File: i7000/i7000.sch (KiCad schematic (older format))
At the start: 31 parts, among them CN04 Conn_02x30_Counter_Clockwise, CN05 Conn_02x07_Counter_Clockwise

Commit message: transcricao de ontem de madrugada
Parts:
- added CI01: 2732, symbol memory:2732
- added CI02: 6116, symbol memory:6116
- added CI06: 74LS240, symbol Logic_74xx:74LS240
- added CI09: 74LS38, symbol Logic_74xx:74LS38
- added CI12: 74LS139, symbol Logic_74xx:74LS139
- added CI13: 74LS273, symbol Logic_74xx:74LS273
- added CI14: 74LS138, symbol Logic_74xx:74LS138
- added CI15: 74LS21, symbol Logic_74xx:74LS21
- added CI16: 74LS123, symbol Logic_74xx:74LS123
- added CI17: 74LS244, symbol Logic_74xx:74LS244
- added CI19: 74LS04, symbol Logic_74xx:74LS04
- added CI21: 74LS00, symbol Logic_74xx:74LS00
- added CN01: Conn_02x30_Counter_Clockwise, symbol Connector:Conn_02x30_Counter_Clockwise
- added CN?: Conn_02x07_Counter_Clockwise, symbol Connector:Conn_02x07_Counter_Clockwise
- added E06: 74LS373, symbol Logic_74xx:74LS373
- added R41: R, symbol device:R
- added U?: 74LS245, symbol Logic_74xx:74LS245
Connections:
- net labels added: CN04_14, CN04_19, CN04_20, CN04_34, CN04_42, CN04_43, CN04_54, CPU_A10, CPU_A11, CPU_A12, CPU_A13, CPU_A14, CPU_A15, CPU_A8, CPU_A9, CPU_AD0, CPU_AD1, CPU_AD2, CPU_AD3, CPU_AD4, CPU_AD5, CPU_AD6, CPU_AD7, ~EPROM_E, ~FDC_CS, ~SRAM_CS, ~WE_CN04_40
- net labels removed: CN04_40
- wire segments 138 -> 272
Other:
- note added: "CI03 (Floppy Controller)\nTODO:\nDesenhar um\nsímbolo para\no WD2793A-PL2"
- note added: "TODO: symbol for NSC800.\nThis one has the Z80 pinout.\nOn the NSC800 the pinout is different."
- moved on the sheet: CN04, CN05, E08, E11, E13, E26B, E27F, E28F, E32C, E36B, F02, F03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

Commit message: mais um pouco hoje
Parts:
- added E02: Intel D8202A-1, symbol chips_not_yet_available_on_kicad:8202A
- added E05: 74LS373, symbol Logic_74xx:74LS373
- added E15: 74LS374, symbol Logic_74xx:74LS374
- added E29: 74LS04, symbol Logic_74xx:74LS04
- added unit 1 of E32
- gave numbers to parts that had none: 2
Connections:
- net labels added: A0, A1, A10, A11, A12, A13, A14, A15, A2, A3, A4, A5, A6, A7, A8, A9, E13_pin2
- net labels removed: CN04_17, DRAM_AH0, DRAM_AH1, DRAM_AH2, DRAM_AH3, DRAM_AH4, DRAM_AH5, DRAM_AL0, DRAM_AL1, DRAM_AL2, DRAM_AL3, DRAM_AL4, DRAM_AL5, DRAM_AL6
- wire segments 272 -> 359
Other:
- note added: "/FDC_CS = 0 when:\nA13 == 1\nA11 == 0\nA10 == 0\nCN04_14 == 0\nCN04_42 == 1\nCN04_43 == 1\n"
- note removed: "E02 (DRAM Controller)\nTODO:\nDesenhar um\nsímbolo para\no Intel D8202A-1"
- moved on the sheet: E09, E10, E13, E32C, E36B

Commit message: creating a library of symbols for chips used in the Itautec I7000 but still not available in KICAD libraries. We should contribute these later to the project.
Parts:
- removed E01: NSC800_CPU, symbol Zilog:Z80CPU
- added E01: NSC800D-4, symbol chips_not_yet_available_on_kicad:NSC800
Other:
- note removed: "TODO: symbol for NSC800.\nThis one has the Z80 pinout.\nOn the NSC800 the pinout is different."
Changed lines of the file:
@@
 	8850 7350 9000 7350
-$Comp
-L Zilog:Z80CPU E01
-U 1 1 5FD1F685
-P 5150 7150
-F 0 "E01" H 5150 8828 50  0000 C CNN
-F 1 "NSC800_CPU" H 5150 8737 50  0000 C CNN
-F 2 "" H 5150 7550 50  0001 C CNN
-F 3 "www.zilog.com/manage_directlink.php?filepath=docs/z80/um0080" H 5150 7550 50  0001 C CNN
-	1    5150 7150
-	1    0    0    -1
-$EndComp
 $Comp
 L Logic_74xx:74LS257 E08
@@
 	1    0    0    -1
 $EndComp
-Text Notes 4750 5450 0    31   ~ 0
-TODO: symbol for NSC800.\nThis one has the Z80 pinout.\nOn the NSC800 the pinout is different.
-Text GLabel 6000 5950 2    31   Output ~ 0
+Text GLabel 4800 5250 0    31   Output ~ 0
 CPU_AD0
 Wire Wire Line
-	5850 5950 6000 5950
-Text GLabel 6000 6050 2    31   Output ~ 0
+	4950 5250 4800 5250
+Text GLabel 4800 5350 0    31   Output ~ 0
 CPU_AD1
-Text GLabel 6000 6150 2    31   Output ~ 0
+Text GLabel 4800 5450 0    31   Output ~ 0
 CPU_AD2
-Text GLabel 6000 6250 2    31   Output ~ 0
+Text GLabel 4800 5550 0    31   Output ~ 0
 CPU_AD3
 Wire Wire Line
-	6000 6050 5850 6050
-Wire Wire Line
-	5850 6150 6000 6150
-Wire Wire Line
-	6000 6250 5850 6250
-Text GLabel 6000 6350 2    31   Output ~ 0
+	4800 5350 4950 5350
+Wire Wire Line
+	4950 5450 4800 5450
+Wire Wire Line
+	4800 5550 4950 5550
+Text GLabel 4800 5650 0    31   Output ~ 0
 CPU_AD4
 Wire Wire Line
-	5850 6350 6000 6350
-Text GLabel 6000 6450 2    31   Output ~ 0
+	4950 5650 4800 5650
+Text GLabel 4800 5750 0    31   Output ~ 0
 CPU_AD5
-Text GLabel 6000 6550 2    31   Output ~ 0
+Text GLabel 4800 5850 0    31   Output ~ 0
 CPU_AD6
-Text GLabel 6000 6650 2    31   Output ~ 0
+Text GLabel 4800 5950 0    31   Output ~ 0
 CPU_AD7
 Wire Wire Line
-	6000 6450 5850 6450
-Wire Wire Line
-	5850 6550 6000 6550
-Wire Wire Line
-	6000 6650 5850 6650
-Text GLabel 6000 6750 2    31   Output ~ 0
+	4800 5750 4950 5750
+Wire Wire Line
+	4950 5850 4800 5850
+Wire Wire Line
+	4800 5950 4950 5950
+Text GLabel 4800 6350 0    31   Output ~ 0
 CPU_A8
 Wire Wire Line
-	5850 6750 6000 6750
-Text GLabel 6000 6850 2    31   Output ~ 0
+	4950 6350 4800 6350
+Text GLabel 4800 6450 0    31   Output ~ 0
 CPU_A9
-Text GLabel 6000 6950 2    31   Output ~ 0
+Text GLabel 4800 6550 0    31   Output ~ 0
 CPU_A10
-Text GLabel 6000 7050 2    31   Output ~ 0
+Text GLabel 4800 6650 0    31   Output ~ 0
 CPU_A11
 Wire Wire Line
-	6000 6850 5850 6850
-Wire Wire Line
-	5850 6950 6000 6950
-Wire Wire Line
-	6000 7050 5850 7050
-Text GLabel 6000 7150 2    31   Output ~ 0
+	4800 6450 4950 6450
+Wire Wire Line
+	4950 6550 4800 6550
+Wire Wire Line
+	4800 6650 4950 6650
+Text GLabel 4800 6750 0    31   Output ~ 0
 CPU_A12
 Wire Wire Line
-	5850 7150 6000 7150
-Text GLabel 6000 7250 2    31   Output ~ 0
+	4950 6750 4800 6750
+Text GLabel 4800 6850 0    31   Output ~ 0
 CPU_A13
-Text GLabel 6000 7350 2    31   Output ~ 0
+Text GLabel 4800 6950 0    31   Output ~ 0
 CPU_A14
-Text GLabel 6000 7450 2    31   Output ~ 0
+Text GLabel 4800 7050 0    31   Output ~ 0
 CPU_A15
 Wire Wire Line
-	6000 7250 5850 7250
-Wire Wire Line
-	5850 7350 6000 7350
-Wire Wire Line
-	6000 7450 5850 7450
+	4800 6850 4950 6850
+Wire Wire Line
+	4950 6950 4800 6950
+Wire Wire Line
+	4800 7050 4950 7050
 Text GLabel 1500 7650 0    31   Input ~ 0
 CPU_AD0
@@
 Text Notes 9900 23650 0    31   ~ 0
 /FDC_CS = 0 when:\nA13 == 1\nA11 == 0\nA10 == 0\nCN04_14 == 0\nCN04_42 == 1\nCN04_43 == 1\n
+$Comp
+L chips_not_yet_available_on_kicad:NSC800 E01
+U 1 1 61F6CA9C
+P 5550 5500
+F 0 "E01" H 5250 6200 31  0000 C CNN
+F 1 "NSC800D-4" H 5750 6200 31  0000 C CNN
+F 2 "" H 5300 6100 31  0001 C CNN
+F 3 "" H 5300 6100 31  0001 C CNN
+	1    5550 5500
+	1    0    0    -1
+$EndComp
 $EndSCHEMATC

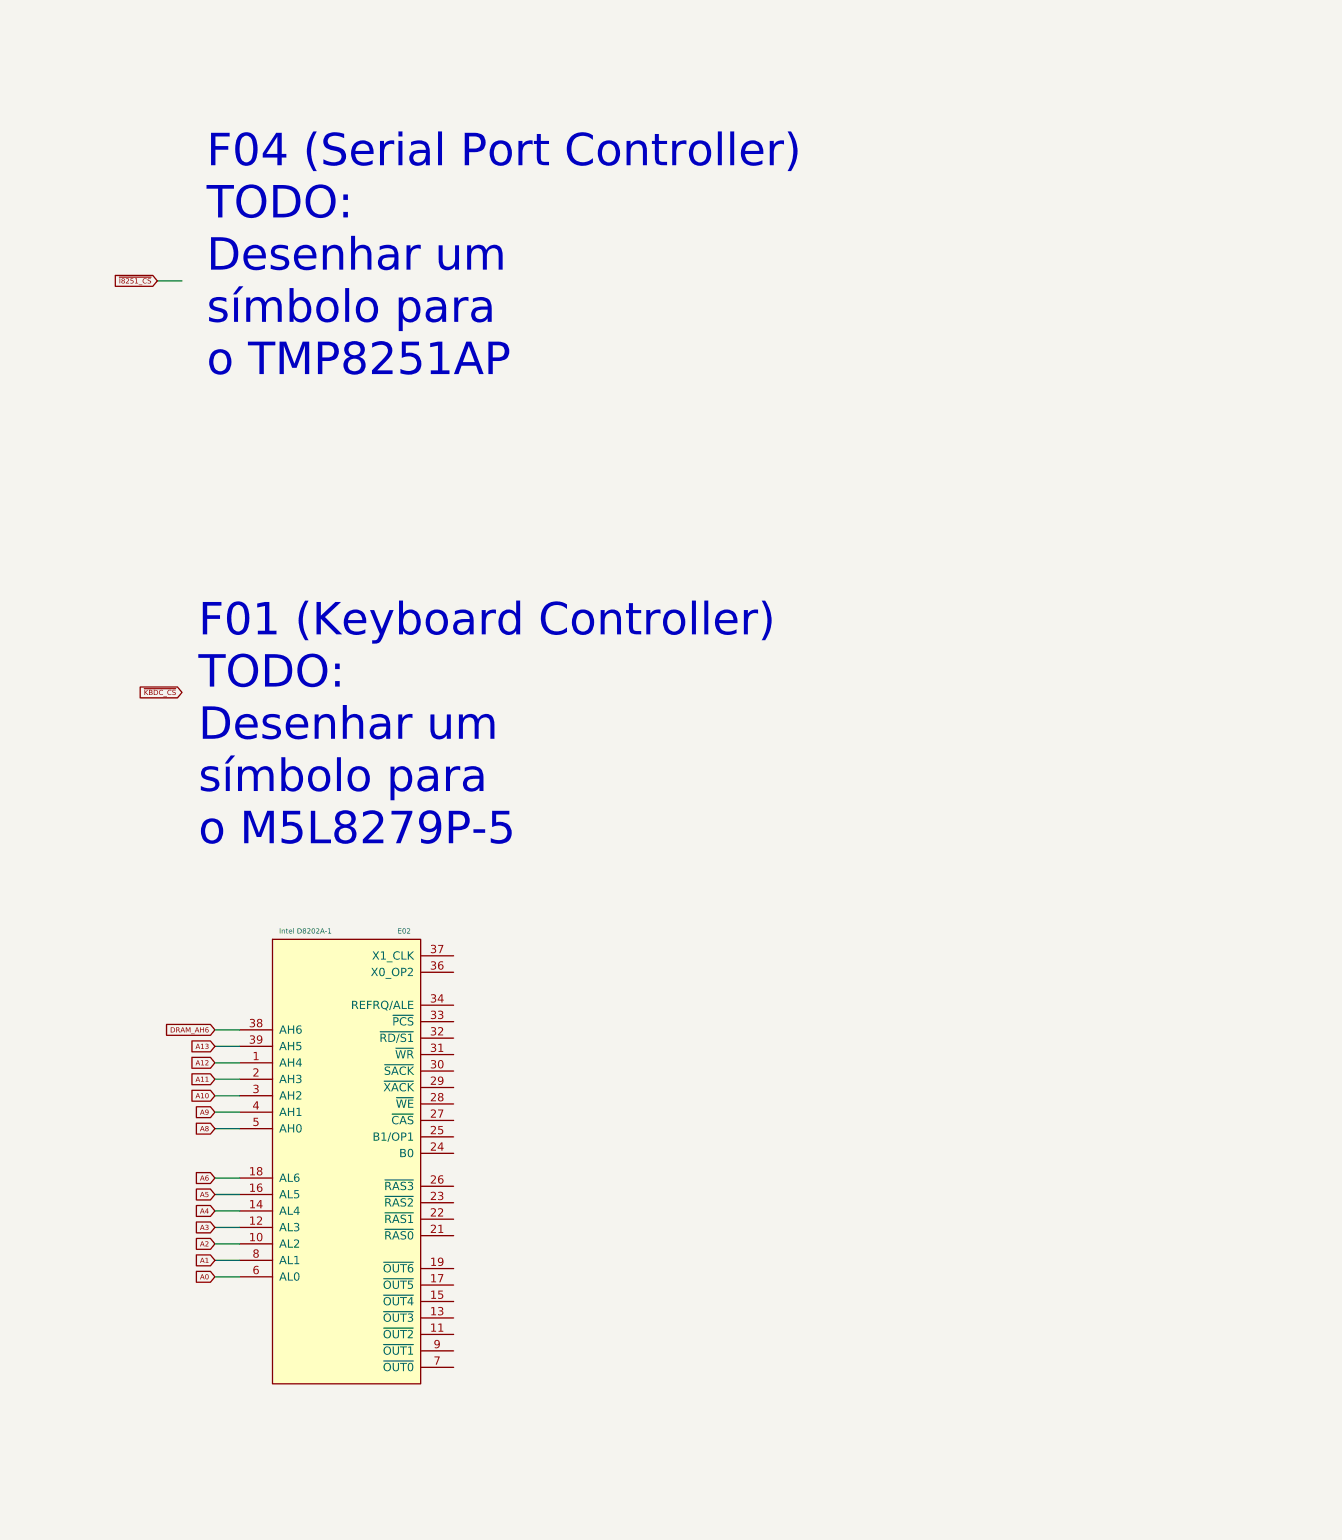
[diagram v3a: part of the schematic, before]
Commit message: Mais um símbolo novo pro KICAD: Programmable Keyboard/display controler M5L8279P-5
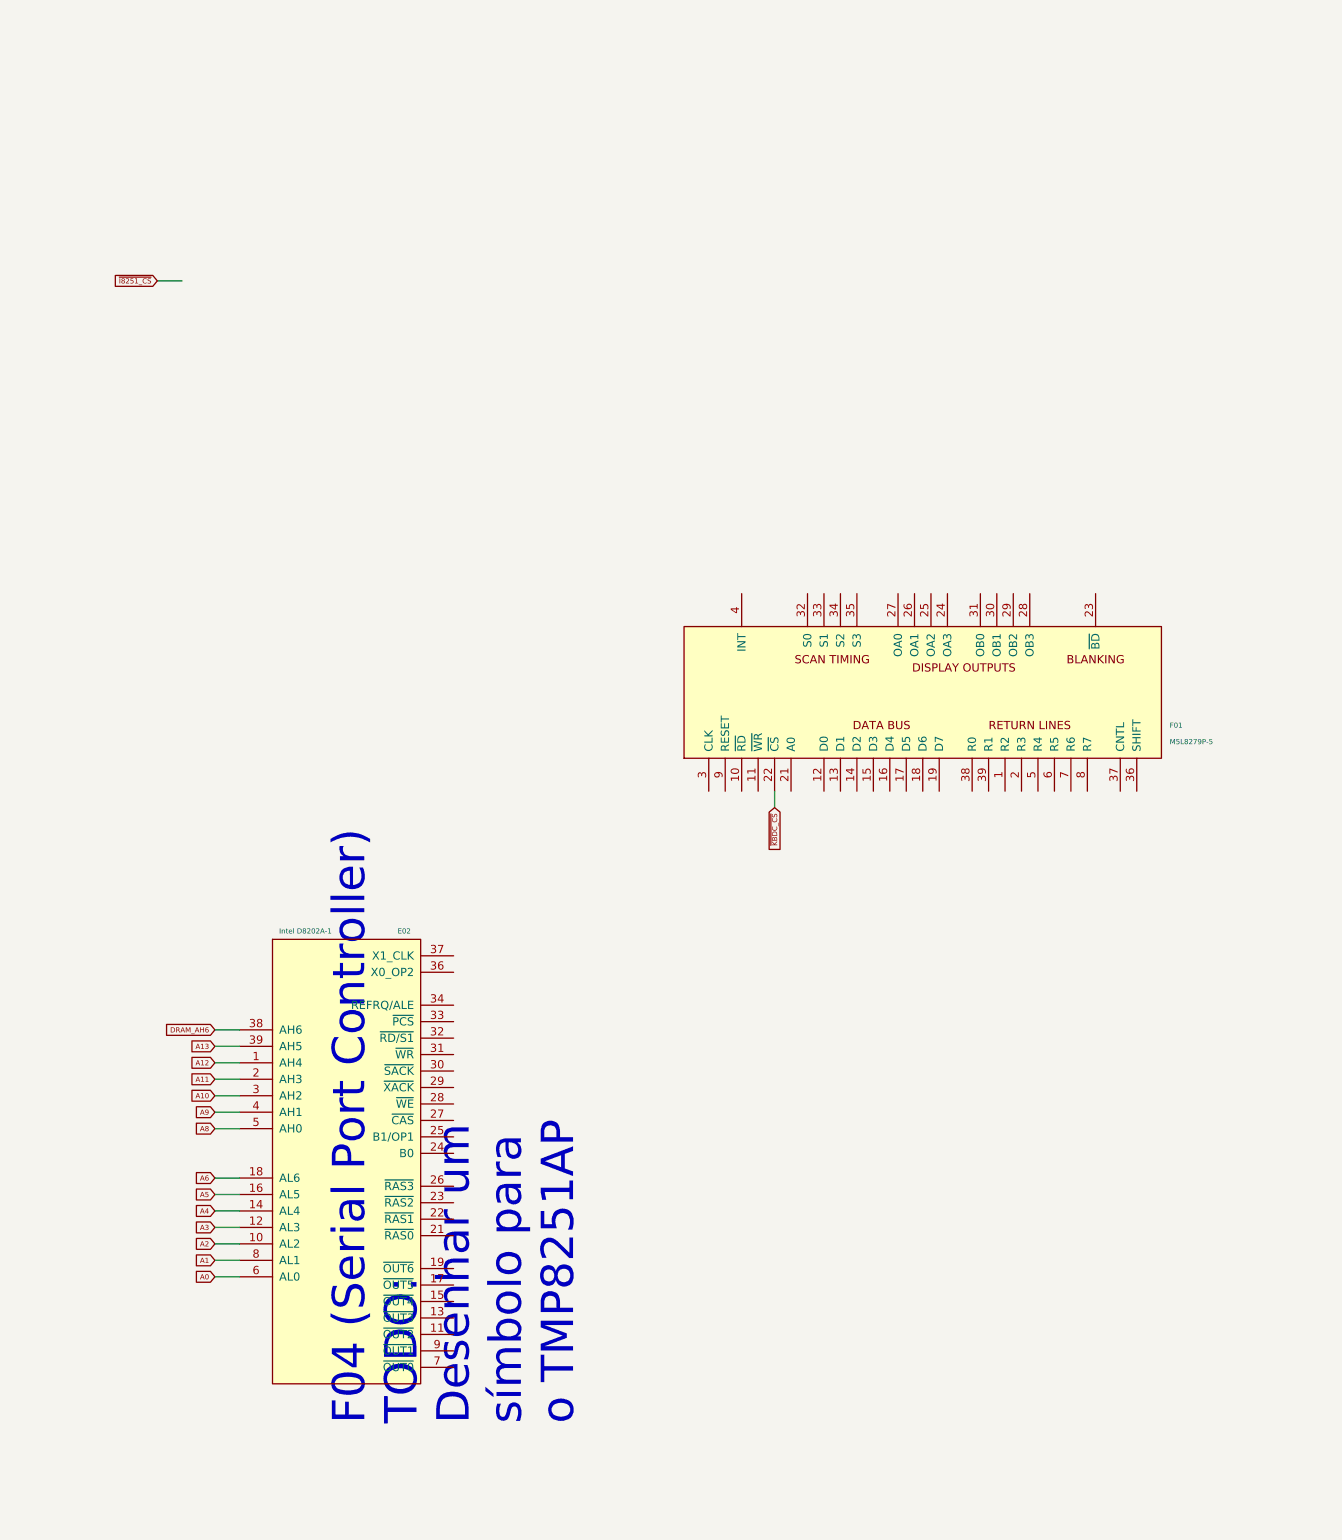
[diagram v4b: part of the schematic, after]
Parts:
- added F01: M5L8279P-5, symbol chips_not_yet_available_on_kicad:M5L8279P-5
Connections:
- net GND: now also F01.20 (GND)
- net VCC: now also F01.40 (VCC)
- net ~KBDC_CS: now also F01.22 (~CS)
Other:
- note removed: "F01 (Keyboard Controller)\nTODO:\nDesenhar um\nsímbolo para\no M5L8279P-5"
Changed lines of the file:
@@
 Wire Wire Line
 	25650 5150 25800 5150
-Text Notes 25950 5750 0    197  ~ 0
+Text Notes 28200 12100 1    197  ~ 0
 F04 (Serial Port Controller)\nTODO:\nDesenhar um\nsímbolo para\no TMP8251AP
 Text GLabel 13600 6250 2    31   Output ~ 0
@@
 Wire Wire Line
 	13600 6150 13250 6150
-Text GLabel 25800 7650 0    31   Input ~ 0
+Text GLabel 29400 8350 3    31   Input ~ 0
 ~KBDC_CS
-Text Notes 25900 8600 0    197  ~ 0
-F01 (Keyboard Controller)\nTODO:\nDesenhar um\nsímbolo para\no M5L8279P-5
 $Comp
 L Logic_74xx:74LS32 G32
@@
 	1    0    0    -1
 $EndComp
+$Comp
+L chips_not_yet_available_on_kicad:M5L8279P-5 F01
+U 1 1 620B6BC7
+P 30250 7650
+F 0 "F01" V 30050 6100 31  0000 R CNN
+F 1 "M5L8279P-5" V 29950 6100 31  0000 R CNN
+F 2 "" H 30550 9050 31  0001 C CNN
+F 3 "" H 30550 9050 31  0001 C CNN
+	1    30250 7650
+	0    -1   -1   0
+$EndComp
+Wire Wire Line
+	29400 8350 29400 8250
 $EndSCHEMATC
